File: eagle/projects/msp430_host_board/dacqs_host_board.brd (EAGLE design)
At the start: 127 x 102 mm, 181 parts, among them J1 MOL-SL-4-RA, J10 MOL-SL-3-V, J11 MOL-SL-2-V, J13 JST-PH-2TH-RA, J14 USB_MICROB_RECPT, J16 MOL-SL-2-RA, J17 CLM-112-02-L-D-IMU-MOUNT_IMU, J18 MOLSL-7-RA, J2 MOL-SL-4-RA, J3 MOL-SL-4-RA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

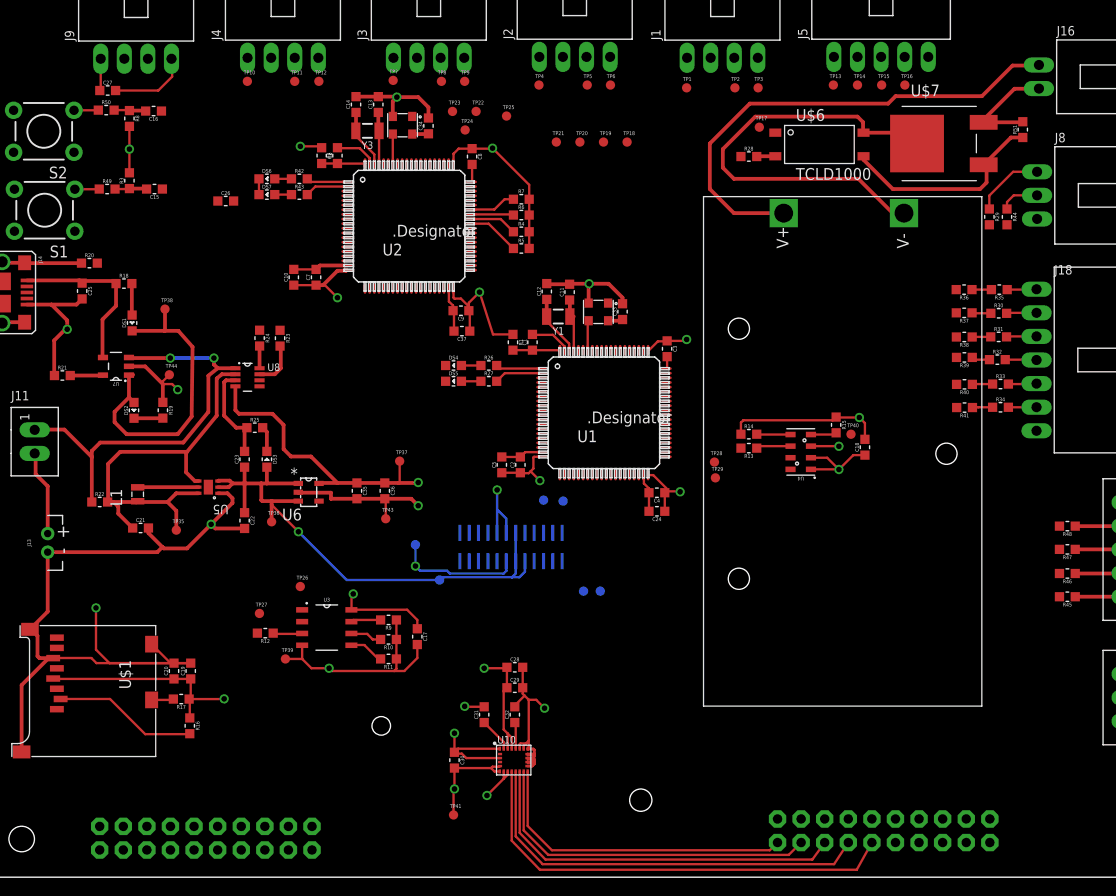
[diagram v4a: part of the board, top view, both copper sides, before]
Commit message: Started routing i2c busses
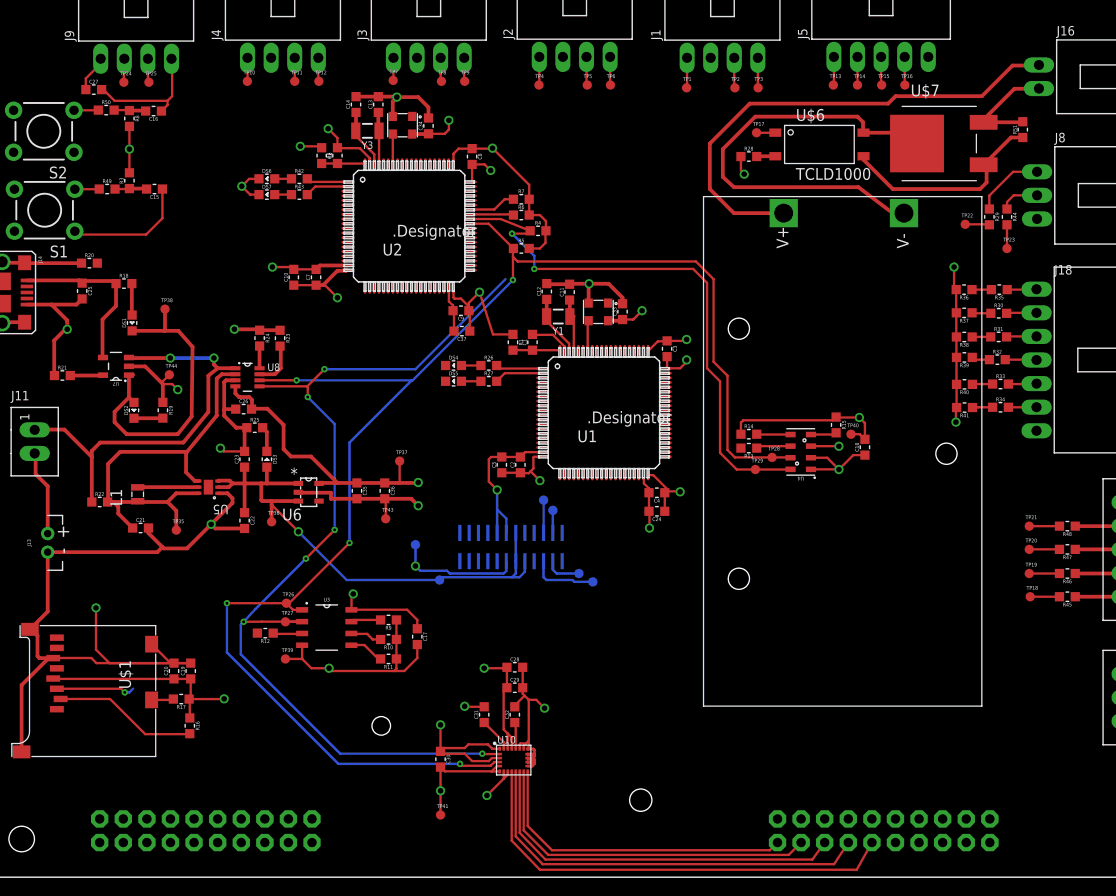
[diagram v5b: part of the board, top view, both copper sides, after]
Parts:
- moved TP21 65.6 mm to (112.3, 37.8)
- moved TP18 65.4 mm to (112.4, 30.2)
- moved TP20 65.3 mm to (112.3, 35.3)
- moved TP19 65.3 mm to (112.3, 32.7)
- moved TP23 61.5 mm to (109.9, 67.7)
- moved TP22 54.1 mm to (105.4, 70.3)
- moved TP25 38.7 mm to (17.5, 85.6)
- moved TP24 37.1 mm to (14.8, 85.6)
- moved C26 22.5 mm to (27.7, 50.4)
- moved TP28 6.22 mm to (84.6, 45.2)
- moved TP29 4.39 mm to (82.8, 43.9)
- moved TP27 2.94 mm to (32.2, 27.5)
- moved TP26 2.34 mm to (32.3, 29.5)
- moved TP30 1.96 mm to (63.8, 32.7)
- moved R4 1.80 mm to (59.4, 69.6)
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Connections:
- net COMMS_MISO_0 renamed EN_MOTOR_OUT_0
- net COMMS_MOSI_0 renamed DIR_MOTOR_OUT_0
- net COMMS_SCLK_0 renamed CURRENT_PWM_OUT_0
- net COMMS_SS_0 renamed SPEED_PWM_OUT_0
- net COMMS_MISO: no longer R47.2, TP20.TP
- net COMMS_MOSI: no longer R48.2, TP21.TP
- net COMMS_SCLK: no longer R46.2, TP19.TP
- net COMMS_SS: no longer R45.2, TP18.TP
- net CURRENT_PWM_OUT: now also R46.2, TP19.TP
- net DIR_MOTOR_OUT: now also R48.2, TP21.TP
- net EN_MOTOR_OUT: now also R47.2, TP20.TP
- net SPEED_PWM_OUT: now also R45.2, TP18.TP
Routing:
- net SENSE_SDA_1: track 5.61 -> 167.6 mm, vias 0 -> 5
- net SENSE_SCL_1: track 5.07 -> 165.8 mm, vias 0 -> 8
- net GND: track 306.6 -> 376.0 mm, vias 15 -> 26
- net +3V3: track 178.3 -> 191.6 mm, vias 15 -> 17
- net SD_MOSI: track 0.00 -> 8.54 mm, vias 0 -> 1
- net IMU_SS: track 0.00 -> 7.24 mm
- net IMU_MISO: track 0.00 -> 3.90 mm
- net IMU_MOSI: track 0.00 -> 3.53 mm
- net UART_1_RX: track 0.00 -> 3.26 mm
- net UART_1_TX: track 0.00 -> 3.25 mm
- net EN_MOTOR_OUT: track 0.00 -> 3.25 mm
- net DIR_MOTOR_OUT: track 0.00 -> 3.25 mm
- net CURRENT_PWM_OUT: track 0.00 -> 3.25 mm
- net RST_PI_1: track 0.00 -> 3.24 mm
- net SPEED_PWM_OUT: track 0.00 -> 3.15 mm
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
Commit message: Added more connections
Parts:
- moved TP31 2.22 mm to (65.6, 34.0)
- moved R7 1.92 mm to (56.4, 74.5), turned to 90 degrees
- moved C37 1.30 mm to (51.2, 57.5)
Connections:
- new net N$6: U2.33
- net SD_CS: no longer U2.33
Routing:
- net SD_CS: track 15.5 -> 190.6 mm, vias 0 -> 2
- net RST_SBWTDIO_HOST: track 3.44 -> 155.2 mm, vias 0 -> 2
- net IMU_RST_1: track 0.00 -> 125.4 mm, vias 0 -> 1
- net IMU_SCLK: track 2.43 -> 126.8 mm, vias 0 -> 1
- net IMU_SS: track 7.24 -> 129.4 mm, vias 0 -> 1
- net SENSE_SDA_2: track 7.08 -> 117.2 mm, vias 0 -> 2
- net SENSE_SCL_2: track 7.55 -> 105.4 mm, vias 0 -> 2
- net SD_SCLK: track 0.00 -> 85.9 mm, vias 0 -> 4
- net UART_3_TX: track 2.44 -> 84.5 mm, vias 0 -> 5
- net SD_MISO: track 0.00 -> 81.6 mm, vias 0 -> 2
- net SD_MOSI: track 8.54 -> 88.3 mm, vias 1 -> 4
- net RST_PI_4: track 2.55 -> 75.2 mm, vias 0 -> 2
- net UART_4_RX: track 2.53 -> 73.8 mm, vias 0 -> 2
- net SD_DETECT: track 2.38 -> 73.4 mm, vias 0 -> 2
- net UART_4_TX: track 2.54 -> 72.5 mm, vias 0 -> 2
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- added copper zone on layer 15, net +3V3
- removed copper zone on layer 3, net +3V3

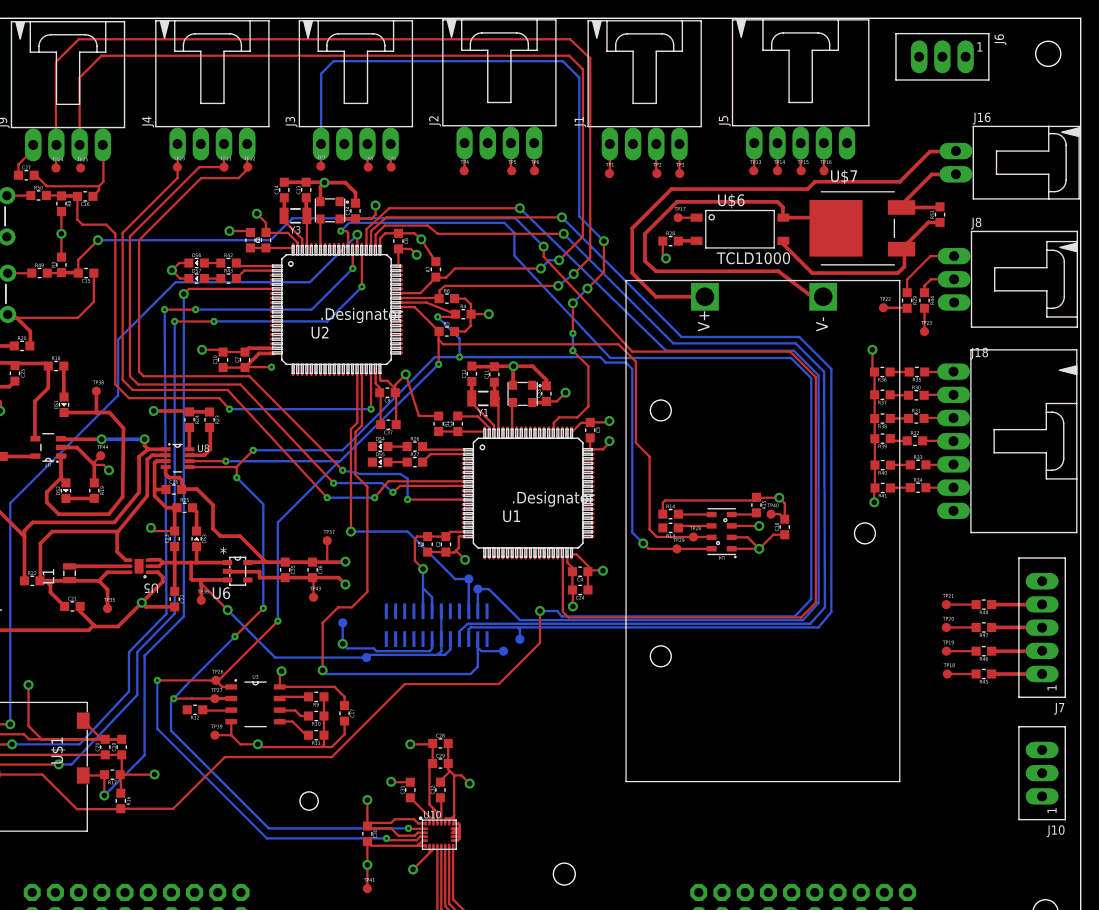
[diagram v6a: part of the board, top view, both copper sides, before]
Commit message: Routed a few more connectors
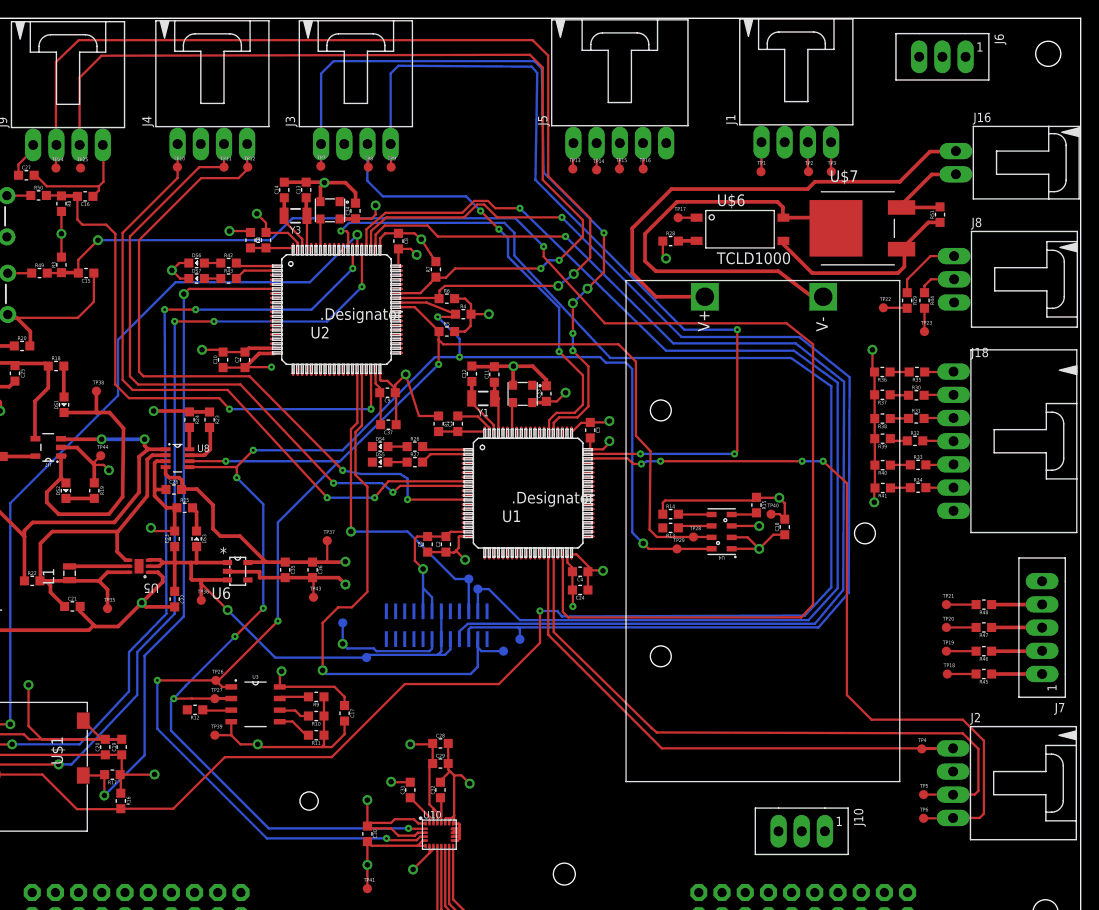
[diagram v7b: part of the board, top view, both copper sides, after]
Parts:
- moved J2 96.5 mm to (120.7, 18.2), turned to 270 degrees
- moved TP6 82.7 mm to (109.8, 14.4)
- moved TP5 81.8 mm to (109.8, 17.0)
- moved TP4 80.7 mm to (109.6, 22.0)
- moved J10 27.1 mm to (96.5, 13.0), turned to 180 degrees
- moved TP15 19.9 mm to (76.5, 85.5)
- moved TP16 19.8 mm to (79.1, 85.5)
- moved TP13 19.8 mm to (71.4, 85.5)
- moved TP14 19.8 mm to (74.0, 85.4)
- moved J5 19.8 mm to (76.5, 96.0)
- moved TP2 16.6 mm to (97.2, 85.2)
- moved TP3 16.6 mm to (99.7, 85.2)
- moved J1 16.6 mm to (95.9, 96.0)
- moved TP1 16.6 mm to (92.0, 85.2)
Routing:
- net RST_PI_3: track 2.55 -> 97.3 mm, vias 0 -> 3
- net RST_PI_2: track 3.05 -> 84.5 mm, vias 0 -> 4
- net UART_2_RX: track 3.06 -> 71.0 mm
- net UART_2_TX: track 3.05 -> 61.8 mm
- net UART_3_RX: track 2.57 -> 52.1 mm, vias 0 -> 3
- net IMU_SCLK: track 126.8 -> 130.0 mm
- net IMU_SS: track 129.4 -> 132.4 mm
- net SD_CS: track 190.6 -> 193.4 mm
- net SENSE_SDA_2: track 117.2 -> 114.6 mm
- net SENSE_SCL_2: track 105.4 -> 103.0 mm
- net IMU_RST_1: track 125.4 -> 127.7 mm
- net UART_3_TX: track 84.5 -> 82.6 mm
- net RST_SBWTDIO_HOST: track 155.2 -> 156.7 mm

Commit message: Finished routing al necessary connectons
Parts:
- moved J6 87.1 mm to (94.3, 12.5)
- moved J8 60.9 mm to (64.2, 96.0), turned to 0 degrees
- moved R29 48.3 mm to (61.6, 84.6)
- moved TP22 48.1 mm to (59.7, 85.4)
- moved R44 47.7 mm to (64.2, 84.6)
- moved TP23 47.0 mm to (66.4, 85.5)
- moved J10 16.6 mm to (79.9, 12.6)
- moved TP17 7.89 mm to (75.6, 83.2)
- moved C36 7.40 mm to (35.5, 41.7)
- moved TP37 6.80 mm to (37.7, 45.0)
- moved C35 6.70 mm to (33.2, 41.7)
- moved C22 6.18 mm to (21.8, 39.9), turned to 180 degrees
- moved TP15 5.90 mm to (82.4, 85.4)
- moved TP13 5.90 mm to (77.3, 85.4)
- moved TP16 5.80 mm to (84.9, 85.4)
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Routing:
- net CURRENT_PWM_OUT: track 3.25 -> 146.1 mm, vias 0 -> 6
- net SPEED_PWM_OUT: track 3.15 -> 135.2 mm, vias 0 -> 8
- net EN_MOTOR_OUT: track 3.25 -> 120.0 mm, vias 0 -> 7
- net DIR_MOTOR_OUT: track 3.25 -> 118.9 mm, vias 0 -> 7
- net VBAT_MOD_CELL_4: track 1.95 -> 95.1 mm, vias 0 -> 2
- net VBAT_MOD_CELL_5: track 2.19 -> 91.6 mm, vias 0 -> 2
- net UART_1_TX: track 3.25 -> 89.4 mm, vias 0 -> 1
- net UART_1_RX: track 3.26 -> 89.0 mm, vias 0 -> 1
- net RST_PI_1: track 3.24 -> 86.0 mm
- net ACT_CURRENT_IN: track 2.55 -> 85.3 mm
- net VBAT_MOD_CELL_6: track 2.17 -> 83.0 mm, vias 0 -> 2
- net SBWTCK_MOTOR: track 0.00 -> 68.5 mm, vias 0 -> 2
- net RST_SBWTDIO_MOTOR: track 60.6 -> 127.4 mm, vias 2 -> 4
- net ACT_SPEED_IN: track 2.62 -> 69.0 mm
- net COMMS_MISO: track 2.85 -> 63.3 mm, vias 0 -> 1
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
